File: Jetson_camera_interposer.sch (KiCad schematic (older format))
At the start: 49 parts, among them J1 QSH-060-01-L-D-A, J2 QTH-060-01-L-D-A, J21 Conn_01x01, J22 Conn_01x01, J23 Conn_01x01, J24 Conn_01x01, J25 Conn_01x01, J26 Conn_01x01, J3 Conn_01x01, J4 Conn_01x01, J5 Conn_01x01, J6 Conn_01x01, T1 TestP, T10 TestP, T11 TestP, T2 TestP, T3 TestP, T5 TestP, T6 TestP, T7 TestP, T8 TestP, T9 TestP

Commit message: good, before updating pcb
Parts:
- FLASH_EN1, GND1, GND2, GND3, GND4, I2C_CLK1, I2C_CLK2, I2C_DAT1, I2C_DAT2, MCLK1, PWR1, RST1, T1, T10, T11, T2, T3, T5, T6, T7, T8, T9, V1.2, V1.8, V3.3, VSYNC1, VSYS1: footprint Test_Point_Keystone_5000-5004_Miniature -> TX2_Footprints:test_point
- J1: footprint hdmi3dmix:samtec-qsh-QSH-060-01-X-D-A -> TX2_Footprints:QSH-060-01-L-D-A
- J2: footprint hdmi3dmix:QTH-060-01-X-D-A-QTH-060-01-X-D-A -> TX2_Footprints:QTH-060-01-L-D-A
- J21, J22, J23, J24, J25, J26, J3, J4, J5, J6: footprint hdmi3dmix:ground_probe -> TX2_Footprints:ground_probe
- R1, R10, R2, R3, R4, R5, R6, R7, R8, R9: footprint Resistors_SMD:R_0805_HandSoldering -> TX2_Footprints:R_0805

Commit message: starting revision 2
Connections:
- net labels added: R_CSI0_CLK_N, R_CSI0_CLK_P, R_CSI0_D0_N, R_CSI0_D0_P, R_CSI0_D1_N, R_CSI0_D1_P, R_CSI1_D0_N, R_CSI1_D0_P, R_CSI1_D1_N, R_CSI1_D1_P
- net labels removed: MUXED_1_CLK_N, MUXED_1_CLK_P, MUXED_1_D0_N, MUXED_1_D0_P, MUXED_1_D1_N, MUXED_1_D1_P, MUXED_1_D2_N, MUXED_1_D2_P, MUXED_1_D3_N, MUXED_1_D3_P
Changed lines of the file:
@@
 Text Label 6800 2750 2    60   ~ 0
 CSI1_D1_N
-Text Label 3000 2050 0    60   ~ 0
-CSI0_D0_P
 Text Label 3000 2150 0    60   ~ 0
 CSI0_D0_N
@@
 $EndComp
 Text Label 7850 2050 0    60   ~ 0
-MUXED_1_D2_P
+R_CSI1_D0_P
 Text Label 7850 2150 0    60   ~ 0
-MUXED_1_D2_N
+R_CSI1_D0_N
 Text Label 7850 2650 0    60   ~ 0
-MUXED_1_D3_P
+R_CSI1_D1_P
 Text Label 7850 2750 0    60   ~ 0
-MUXED_1_D3_N
+R_CSI1_D1_N
 Text Label 1500 2050 0    60   ~ 0
-MUXED_1_D0_P
+R_CSI0_D0_P
 Text Label 1500 2150 0    60   ~ 0
-MUXED_1_D0_N
+R_CSI0_D0_N
 Text Label 1500 2350 0    60   ~ 0
-MUXED_1_CLK_P
+R_CSI0_CLK_P
 Text Label 1500 2450 0    60   ~ 0
-MUXED_1_CLK_N
+R_CSI0_CLK_N
 Text Label 1500 2650 0    60   ~ 0
-MUXED_1_D1_P
+R_CSI0_D1_P
 Text Label 1500 2750 0    60   ~ 0
-MUXED_1_D1_N
+R_CSI0_D1_N
 NoConn ~ 5900 3250
 NoConn ~ 5900 3350
@@
 NoConn ~ 5900 3650
 Text Label 12150 2050 0    60   ~ 0
-MUXED_1_D2_P
+R_CSI1_D0_P
 Text Label 12150 2150 0    60   ~ 0
-MUXED_1_D2_N
+R_CSI1_D0_N
 Text Label 12100 2650 0    60   ~ 0
-MUXED_1_D3_P
+R_CSI1_D1_P
 Text Label 12100 2750 0    60   ~ 0
-MUXED_1_D3_N
+R_CSI1_D1_N
 Text Label 8800 2050 0    60   ~ 0
-MUXED_1_D0_P
+R_CSI0_D0_P
 Text Label 8800 2150 0    60   ~ 0
-MUXED_1_D0_N
+R_CSI0_D0_N
 Text Label 8800 2350 0    60   ~ 0
-MUXED_1_CLK_P
+R_CSI0_CLK_P
 Text Label 8800 2450 0    60   ~ 0
-MUXED_1_CLK_N
+R_CSI0_CLK_N
 Text Label 8800 2650 0    60   ~ 0
-MUXED_1_D1_P
+R_CSI0_D1_P
 Text Label 8800 2750 0    60   ~ 0
-MUXED_1_D1_N
+R_CSI0_D1_N
 $Comp
 L TX2_Symbols:Conn_01x01 J3
@@
 	1    0    0    -1
 $EndComp
+Text Label 3000 2050 0    60   ~ 0
+CSI0_D0_P
 $EndSCHEMATC

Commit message: more schematic editing
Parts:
- removed R1, R10, R2, R3, R4, R5, R6, R7, R8, R9: 0, TX2_Footprints:R_0805, symbol TX2_Symbols:R
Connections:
- net labels added: CSI2_CLK_N, CSI2_CLK_P, CSI2_D0_N, CSI2_D0_P, CSI2_D1_N, CSI2_D1_P, CSI3_CLK_N, CSI3_CLK_P, CSI3_D0_N, CSI3_D0_P, CSI3_D1_N, CSI3_D1_P, CSI4_CLK_N, CSI4_CLK_P, CSI4_D0_N, CSI4_D0_P, CSI4_D1_N, CSI4_D1_P, CSI5_CLK_N, CSI5_CLK_P, CSI5_D0_N, CSI5_D0_P, CSI5_D1_N, CSI5_D1_P
- net labels removed: R_CSI0_CLK_N, R_CSI0_CLK_P, R_CSI0_D0_N, R_CSI0_D0_P, R_CSI0_D1_N, R_CSI0_D1_P, R_CSI1_D0_N, R_CSI1_D0_P, R_CSI1_D1_N, R_CSI1_D1_P
- wire segments 249 -> 287
- no-connect marks 113 -> 65

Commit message: done schematic
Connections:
- net CSI1_CLK_N: now reaches J2.10 (CSI1_CLK_N)
- net CSI1_CLK_N: now also J1.10 (CSI1_CLK_N)
- net I2S3_CLK: now reaches J2.72 (I2S3_CLK)
- net I2S3_CLK: now also J1.72 (I2S3_CLK)
- net I2S3_LRCLK: now reaches J2.74 (I2S3_LRCLK)
- net I2S3_LRCLK: now also J1.74 (I2S3_LRCLK)
- net I2S3_SDIN: now reaches J2.76 (I2S3_SDIN)
- net I2S3_SDIN: now also J1.76 (I2S3_SDIN)
- net I2S3_SDOUT: now reaches J2.78 (I2S3_SDOUT)
- net I2S3_SDOUT: now also J1.78 (I2S3_SDOUT)
- net CSI1_CLK_P: now reaches J2.8 (CSI1_CLK_P)
- net CSI1_CLK_P: now also J1.8 (CSI1_CLK_P)
- net CAM_I2C2_SCL: now reaches J2.87 (CAM_I2C2_SCL)
- net CAM_I2C2_SCL: now also J1.87 (CAM_I2C2_SCL)
- net CAM1_MCLK: now reaches J2.88 (CAM1_MCLK)
- net CAM1_MCLK: now also J1.88 (CAM1_MCLK)
- net CAM_I2C2_SDA: now reaches J2.89 (CAM_I2C2_SDA)
- net CAM_I2C2_SDA: now also J1.89 (CAM_I2C2_SDA)
- net CAM1_PWDN: now reaches J2.90 (CAM1_PWDN)
- net CAM1_PWDN: now also J1.90 (CAM1_PWDN)
- net CAM1_RST_L: now reaches J2.92 (CAM1_RST_L)
- net CAM1_RST_L: now also J1.92 (CAM1_RST_L)
- net CAM2_MCLK: now reaches J2.94 (CAM2_MCLK)
- net CAM2_MCLK: now also J1.94 (CAM2_MCLK)
- net CAM2_PWDN: now reaches J2.96 (CAM2_PWDN)
- net CAM2_PWDN: now also J1.96 (CAM2_PWDN)
- net CAM2_RST: now reaches J2.98 (CAM2_RST)
- net CAM2_RST: now also J1.98 (CAM2_RST)
- no-connect marks 65 -> 37
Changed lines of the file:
@@
 Comment4 ""
 $EndDescr
-$Comp
-L TX2_Symbols:QTH-060-01-L-D-A J2
-U 1 1 595ACB35
-P 4800 5050
-F 0 "J2" H 4450 1350 45  0000 L BNN
-F 1 "QTH-060-01-L-D-A" H 4450 8200 45  0000 L BNN
-F 2 "TX2_Footprints:QTH-060-01-L-D-A" H 4480 8200 20  0001 C CNN
-F 3 "" H 4450 8050 60  0001 C CNN
-	1    4800 5050
-	1    0    0    -1
-$EndComp
 Text Notes 8900 10700 0    118  ~ 24
 Stackup:\nSingle Ended: 6 mil\nDifferential:\n4  mil Width, 8 mil spacing\n-----\n0.1 mm height to ground plane\n
@@
 $EndComp
 NoConn ~ 4250 7250
-NoConn ~ 4250 6450
-NoConn ~ 4250 6550
 NoConn ~ 4250 4950
 NoConn ~ 4250 5150
@@
 NoConn ~ 5900 7650
 NoConn ~ 5900 7750
-NoConn ~ 5900 6450
-NoConn ~ 5900 6550
-NoConn ~ 5900 6650
-NoConn ~ 5900 5650
-NoConn ~ 5900 5750
-NoConn ~ 5900 5850
-NoConn ~ 5900 5950
 NoConn ~ 5900 5150
 NoConn ~ 5900 5250
@@
 	1    0    0    -1
 $EndComp
-NoConn ~ 5900 2350
-NoConn ~ 5900 2450
-NoConn ~ 11500 2350
-NoConn ~ 11500 2450
 Text Notes 3200 10600 0    98   ~ 20
 Diff pairs length:\nMuxed1_clk = 79.193 + 47.282 = 126.475\nMuxed1_D0  = 45.339 + 74.459 = 126.475\nMuxed1_D1  = 83.195  + 43.28  = 126.475\nMuxed1_D2  = 30  + 96.475  =  126.475\nMuxed1_D3  = 26.7 + 79.356 = 126.475
@@
 	1    0    0    -1
 $EndComp
-NoConn ~ 11500 6450
-NoConn ~ 11500 6550
-NoConn ~ 11500 6650
-NoConn ~ 5900 6750
-NoConn ~ 5900 6850
-NoConn ~ 5900 6950
-NoConn ~ 11500 6750
-NoConn ~ 11500 6850
-NoConn ~ 11500 6950
 NoConn ~ 11500 7250
 NoConn ~ 11500 7350
@@
 NoConn ~ 9850 5650
 NoConn ~ 9850 5750
-NoConn ~ 9850 6450
-NoConn ~ 9850 6550
 Text Label 9150 5850 2    60   ~ 0
 I2C_CAM_CLK
@@
 NoConn ~ 11500 5450
 NoConn ~ 11500 5550
-NoConn ~ 11500 5650
-NoConn ~ 11500 5750
-NoConn ~ 11500 5850
-NoConn ~ 11500 5950
 Text Label 8900 4750 0    60   ~ 0
 DVDD_CAM_LV
@@
 Text Label 3000 4550 0    60   ~ 0
 CSI4_D1_N
-$Comp
-L TX2_Symbols:QSH-060-01-L-D-A J1
-U 1 1 5A5122D0
-P 10400 5050
-F 0 "J1" H 10050 1850 45  0000 L BNN
-F 1 "QSH-060-01-L-D-A" H 10050 8200 45  0000 L BNN
-F 2 "TX2_Footprints:QSH-060-01-L-D-A" H 10080 8200 20  0001 C CNN
-F 3 "" H 10050 8050 60  0001 C CNN
-	1    10400 5050
-	1    0    0    -1
-$EndComp
 Wire Wire Line
 	11500 2950 12100 2950
@@
 Text Label 6800 4550 0    60   ~ 0
 CSI5_D1_N
+Wire Wire Line
+	11500 6450 12100 6450
+Wire Wire Line
+	11500 6550 12100 6550
+Wire Wire Line
+	11500 6650 12100 6650
+Wire Wire Line
+	11500 6750 12100 6750
+Wire Wire Line
+	11500 6850 12100 6850
+Wire Wire Line
+	11500 6950 12100 6950
+Text Label 12100 6450 0    60   ~ 0
+CAM1_MCLK
+Text Label 12100 6550 0    60   ~ 0
+CAM1_PWDN
+Text Label 12100 6650 0    60   ~ 0
+CAM1_RST_L
+Text Label 12100 6750 0    60   ~ 0
+CAM2_MCLK
+Text Label 12100 6850 0    60   ~ 0
+CAM2_PWDN
+Text Label 12100 6950 0    60   ~ 0
+CAM2_RST
+$Comp
+L TX2_Symbols:QTH-060-01-L-D-A J2
+U 1 1 595ACB35
+P 4800 5050
+F 0 "J2" H 4450 1350 45  0000 L BNN
+F 1 "QTH-060-01-L-D-A" H 4450 8200 45  0000 L BNN
+F 2 "TX2_Footprints:QTH-060-01-L-D-A" H 4480 8200 20  0001 C CNN
+F 3 "" H 4450 8050 60  0001 C CNN
+	1    4800 5050
+	1    0    0    -1
+$EndComp
+Wire Wire Line
+	5900 6450 6500 6450
+Wire Wire Line
+	5900 6550 6500 6550
+Wire Wire Line
+	5900 6650 6500 6650
+Wire Wire Line
+	5900 6750 6500 6750
+Wire Wire Line
+	5900 6850 6500 6850
+Wire Wire Line
+	5900 6950 6500 6950
+Text Label 6500 6450 0    60   ~ 0
+CAM1_MCLK
+Text Label 6500 6550 0    60   ~ 0
+CAM1_PWDN
+Text Label 6500 6650 0    60   ~ 0
+CAM1_RST_L
+Text Label 6500 6750 0    60   ~ 0
+CAM2_MCLK
+Text Label 6500 6850 0    60   ~ 0
+CAM2_PWDN
+Text Label 6500 6950 0    60   ~ 0
+CAM2_RST
+Wire Wire Line
+	8700 6450 9850 6450
+Wire Wire Line
+	9850 6550 8700 6550
+Text Label 8700 6450 0    60   ~ 0
+CAM_I2C2_SCL
+Text Label 8700 6550 0    60   ~ 0
+CAM_I2C2_SDA
+Wire Wire Line
+	4250 6450 2700 6450
+Wire Wire Line
+	4250 6550 2700 6550
+Text Label 2700 6450 0    60   ~ 0
+CAM_I2C2_SCL
+Text Label 2700 6550 0    60   ~ 0
+CAM_I2C2_SDA
+Wire Wire Line
+	11500 2350 12150 2350
+Wire Wire Line
+	11500 2450 12150 2450
+Text Label 12150 2350 0    60   ~ 0
+CSI1_CLK_P
+Text Label 12150 2450 0    60   ~ 0
+CSI1_CLK_N
+Wire Wire Line
+	5900 2350 6800 2350
+Wire Wire Line
+	5900 2450 6800 2450
+Text Label 6800 2350 0    60   ~ 0
+CSI1_CLK_P
+Text Label 6800 2450 0    60   ~ 0
+CSI1_CLK_N
+$Comp
+L TX2_Symbols:QSH-060-01-L-D-A J1
+U 1 1 5A5122D0
+P 10400 5050
+F 0 "J1" H 10050 1850 45  0000 L BNN
+F 1 "QSH-060-01-L-D-A" H 10050 8200 45  0000 L BNN
+F 2 "TX2_Footprints:QSH-060-01-L-D-A" H 10080 8200 20  0001 C CNN
+F 3 "" H 10050 8050 60  0001 C CNN
+	1    10400 5050
+	1    0    0    -1
+$EndComp
+Wire Wire Line
+	11500 5650 12150 5650
+Wire Wire Line
+	11500 5750 12150 5750
+Wire Wire Line
+	11500 5850 12150 5850
+Wire Wire Line
+	11500 5950 12150 5950
+Text Label 12150 5650 0    60   ~ 0
+I2S3_CLK
+Text Label 12150 5750 0    60   ~ 0
+I2S3_LRCLK
+Text Label 12150 5850 0    60   ~ 0
+I2S3_SDIN
+Text Label 12150 5950 0    60   ~ 0
+I2S3_SDOUT
+Wire Wire Line
+	5900 5650 6500 5650
+Wire Wire Line
+	5900 5750 6500 5750
+Wire Wire Line
+	5900 5850 6500 5850
+Wire Wire Line
+	5900 5950 6500 5950
+Text Label 6500 5650 0    60   ~ 0
+I2S3_CLK
+Text Label 6500 5750 0    60   ~ 0
+I2S3_LRCLK
+Text Label 6500 5850 0    60   ~ 0
+I2S3_SDIN
+Text Label 6500 5950 0    60   ~ 0
+I2S3_SDOUT
 $EndSCHEMATC

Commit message: Added debug connector
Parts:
- removed FLASH_EN1, I2C_CLK1, I2C_DAT1, MCLK1, PWR1, RST1, T1, T10, T11, T2, T3, T5, T6, T7, T8, T9, V1.2, V1.8, V3.3, VSYNC1, VSYS1: TestP, TX2_Footprints:test_point, symbol TX2_Symbols:TEST_1P
- added J7: Conn_02x10_Odd_Even, Pin_Headers:Pin_Header_Straight_2x10_Pitch2.54mm, symbol Connector_Generic:Conn_02x10_Odd_Even
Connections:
- net labels added: AVDD_CAM_J, DVDD_CAM_LV_J, JETSON_1V2_J, JETSON_1V8_J, VDD_3V3_J, VDD_AF_J, VDD_CAM_FQ_HV_CAM_J, VDD_IR_J, VDD_SYS_J
- wire segments 315 -> 331
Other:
- moved on the sheet: GND1, GND2, GND3, GND4, I2C_CLK2, I2C_DAT2, J1, J2, J21, J22, J23, J24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

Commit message: routing
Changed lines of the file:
@@
 	13350 7900 13850 7900
 Text Label 11850 7900 0    60   ~ 0
-VDD_SYS
+VDD_SYS_J
 Text Label 11850 8000 0    60   ~ 0
-VDD_IR
+VDD_IR_J
 Text Label 11850 8100 0    60   ~ 0
 VDD_3V3
@@
 	13850 8800 13850 8950
 Text Label 13850 7900 0    60   ~ 0
-VDD_SYS_J
+VDD_SYS
 Text Label 13850 8000 0    60   ~ 0
-VDD_IR_J
+VDD_IR
 Text Label 13850 8100 0    60   ~ 0
 VDD_3V3_J

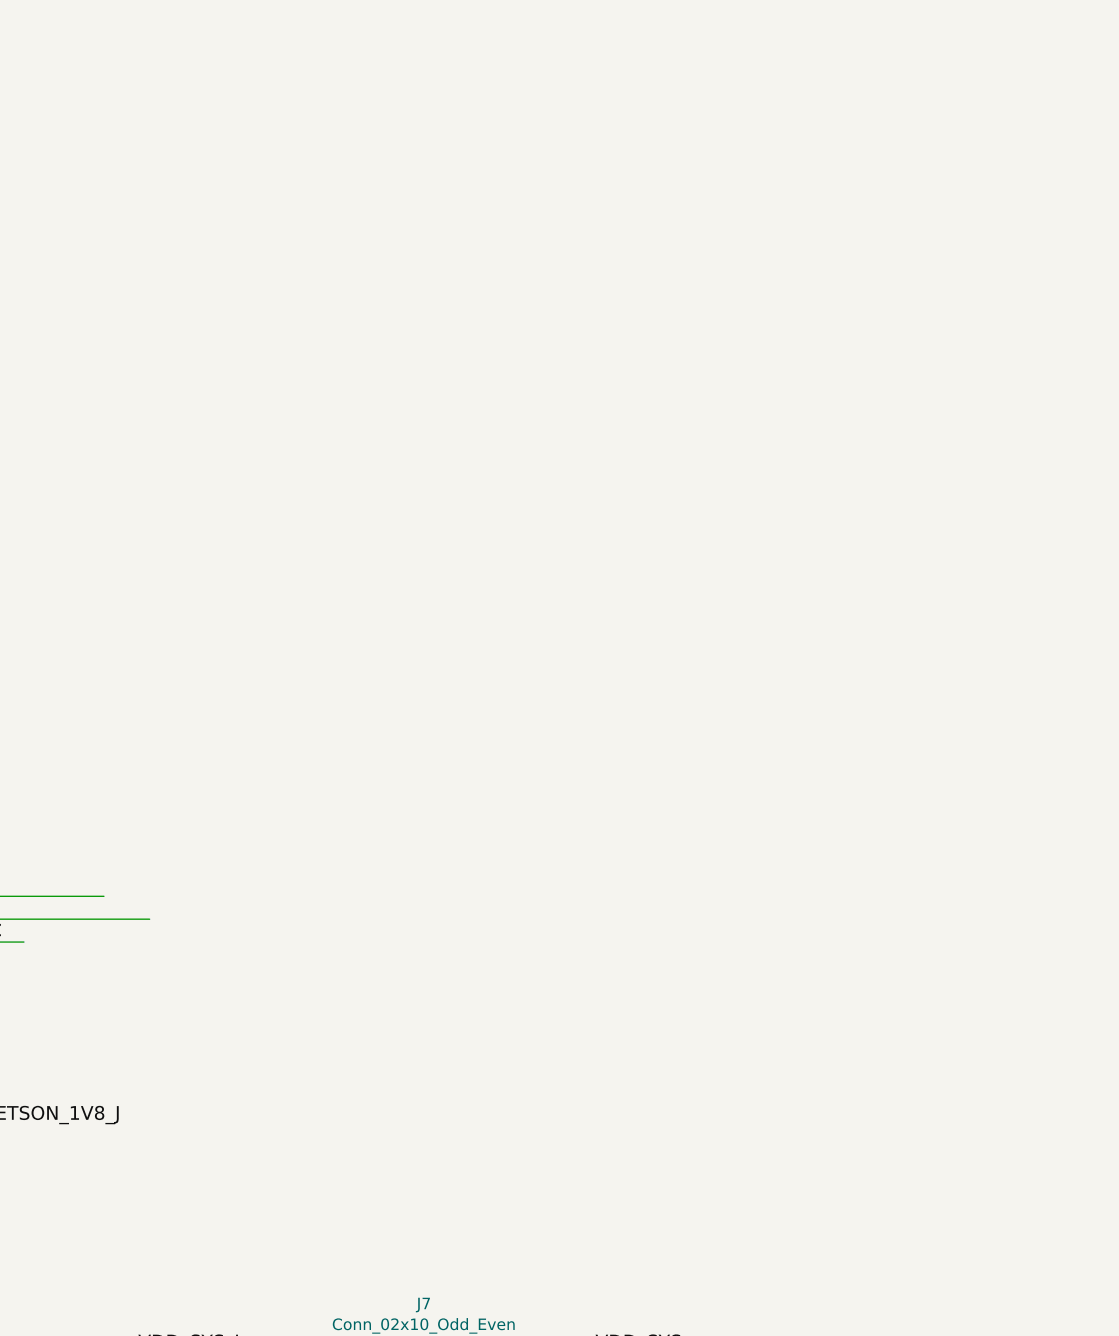
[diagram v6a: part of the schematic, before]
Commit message: good, before changing footprint
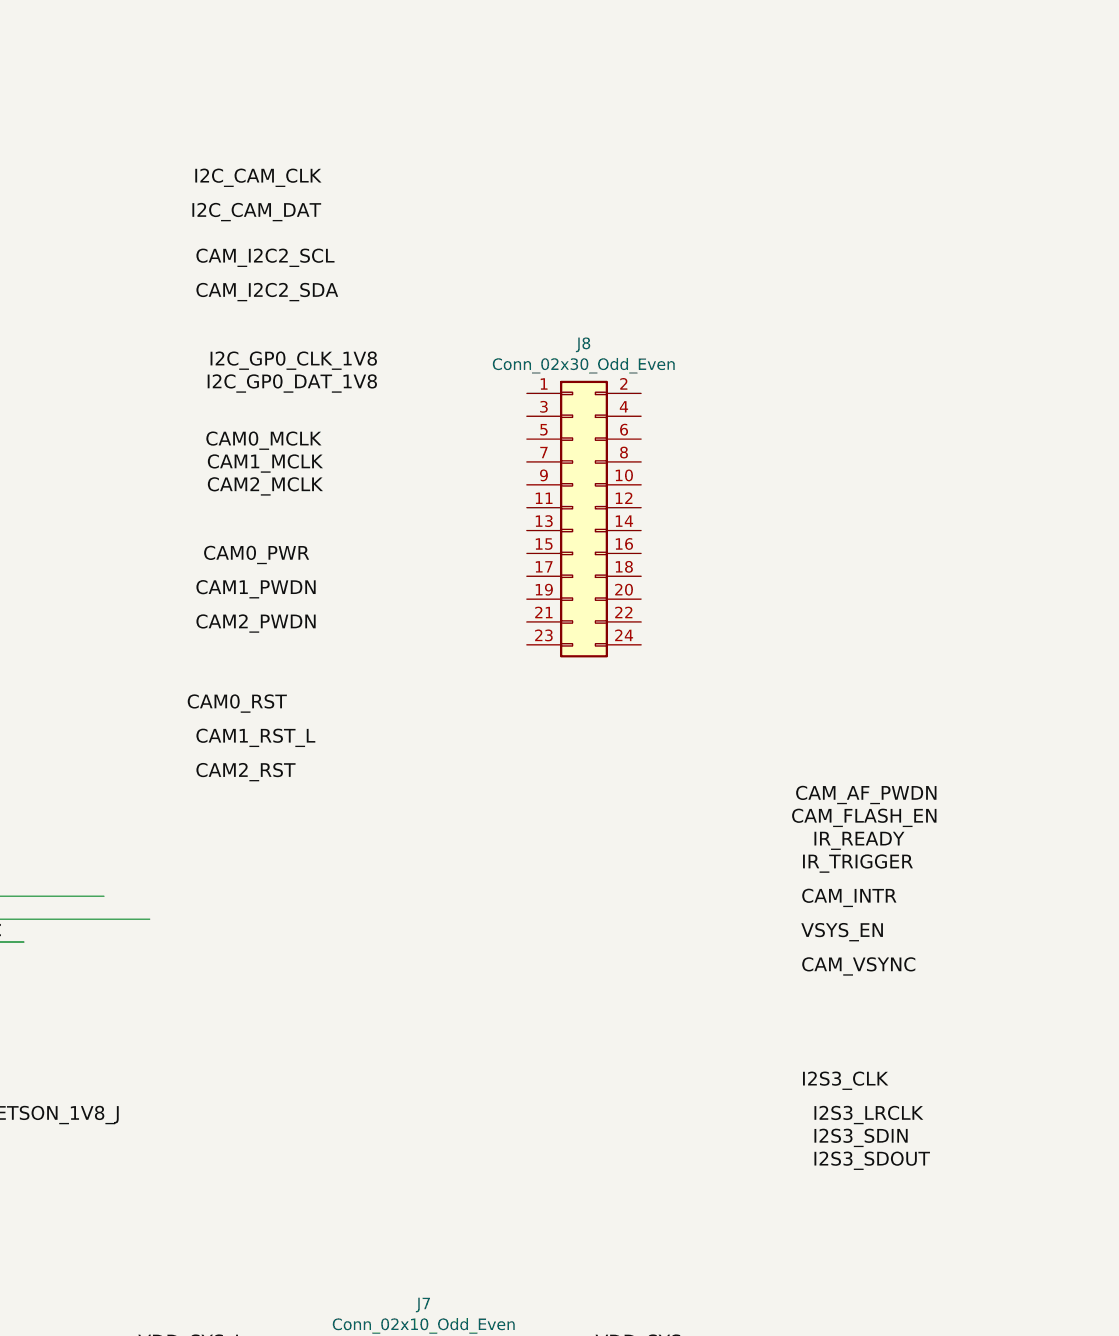
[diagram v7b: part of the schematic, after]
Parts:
- added J8: Conn_02x30_Odd_Even, Pin_Headers:Pin_Header_Straight_2x12_Pitch2.54mm, symbol Connector_Generic:Conn_02x12_Odd_Even
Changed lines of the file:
@@
 Wire Wire Line
 	9800 7700 10200 7700
+Text Label 12650 2800 2    60   ~ 0
+I2C_CAM_CLK
+Text Label 12650 2950 2    60   ~ 0
+I2C_CAM_DAT
+Text Label 15350 5500 2    60   ~ 0
+CAM_AF_PWDN
+Text Label 12100 3150 0    60   ~ 0
+CAM_I2C2_SCL
+Text Label 12100 3300 0    60   ~ 0
+CAM_I2C2_SDA
+Text Label 12650 3950 2    60   ~ 0
+CAM0_MCLK
+Text Label 12600 4450 2    60   ~ 0
+CAM0_PWR
+Text Label 15350 5600 2    60   ~ 0
+CAM_FLASH_EN
+Text Label 12900 3600 2    60   ~ 0
+I2C_GP0_CLK_1V8
+Text Label 12900 3700 2    60   ~ 0
+I2C_GP0_DAT_1V8
+Text Label 14800 5700 0    60   ~ 0
+IR_READY
+Text Label 14750 5800 0    60   ~ 0
+IR_TRIGGER
+Text Label 14750 5950 0    60   ~ 0
+CAM_INTR
+Text Label 14750 6100 0    60   ~ 0
+VSYS_EN
+Text Label 14750 6750 0    60   ~ 0
+I2S3_CLK
+Text Label 14800 6900 0    60   ~ 0
+I2S3_LRCLK
+Text Label 14800 7000 0    60   ~ 0
+I2S3_SDIN
+Text Label 14800 7100 0    60   ~ 0
+I2S3_SDOUT
+Text Label 14750 6250 0    60   ~ 0
+CAM_VSYNC
+Text Label 12150 4050 0    60   ~ 0
+CAM1_MCLK
+Text Label 12100 4600 0    60   ~ 0
+CAM1_PWDN
+Text Label 12100 5250 0    60   ~ 0
+CAM1_RST_L
+Text Label 12150 4150 0    60   ~ 0
+CAM2_MCLK
+Text Label 12100 4750 0    60   ~ 0
+CAM2_PWDN
+Text Label 12100 5400 0    60   ~ 0
+CAM2_RST
+Text Label 12500 5100 2    60   ~ 0
+CAM0_RST
+$Comp
+L Connector_Generic:Conn_02x12_Odd_Even J8
+U 1 1 6174E2F6
+P 13750 4200
+F 0 "J8" H 13800 4917 50  0000 C CNN
+F 1 "Conn_02x30_Odd_Even" H 13800 4826 50  0000 C CNN
+F 2 "Pin_Headers:Pin_Header_Straight_2x12_Pitch2.54mm" H 13750 4200 50  0001 C CNN
+F 3 "~" H 13750 4200 50  0001 C CNN
+	1    13750 4200
+	1    0    0    -1
+$EndComp
 $EndSCHEMATC
